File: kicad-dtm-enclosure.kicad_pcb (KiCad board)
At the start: 2 copper layers, 82.6 x 101.6 mm, 1 part, among them J1 DTM13-12PA-R008_TEC

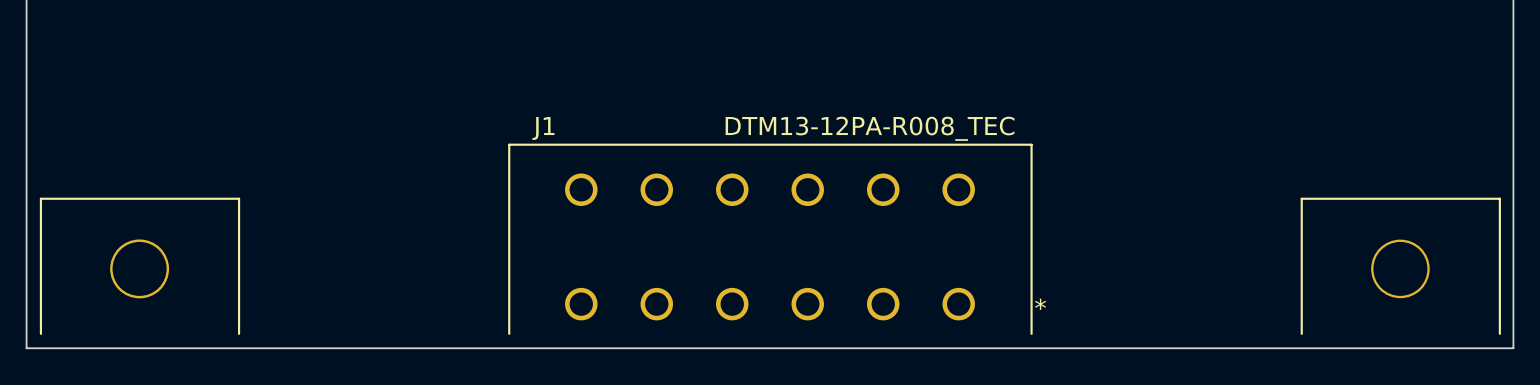
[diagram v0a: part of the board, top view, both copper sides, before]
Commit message: fix footprint reference
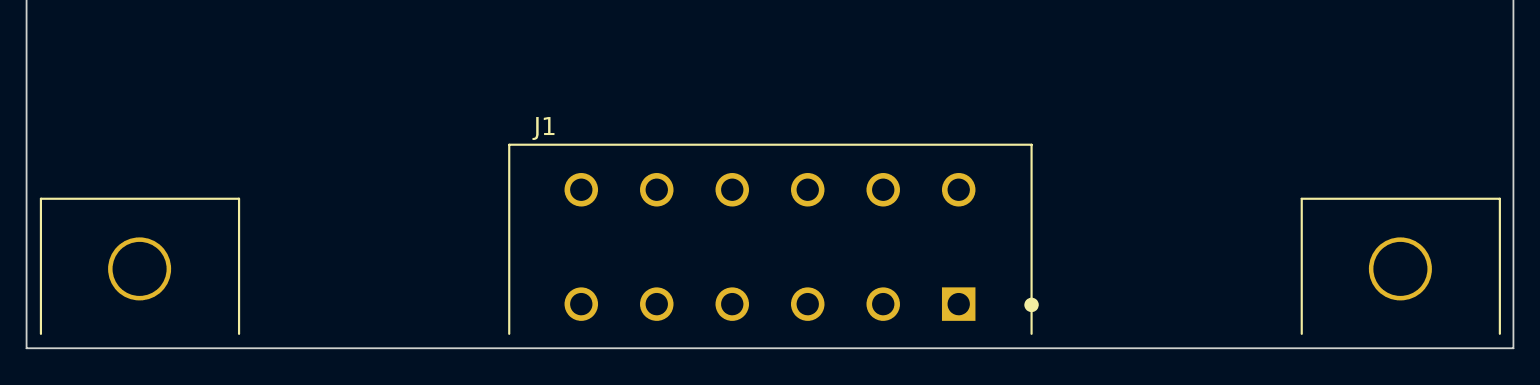
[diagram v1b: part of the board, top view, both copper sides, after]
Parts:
- J1: footprint lib_fp:DTM13-12Px-R008 -> kicad-dtm-enclosure:DTM13-12Px-R008
